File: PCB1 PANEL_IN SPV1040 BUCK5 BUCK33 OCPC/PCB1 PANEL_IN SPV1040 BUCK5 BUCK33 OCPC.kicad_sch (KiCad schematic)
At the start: 0 parts

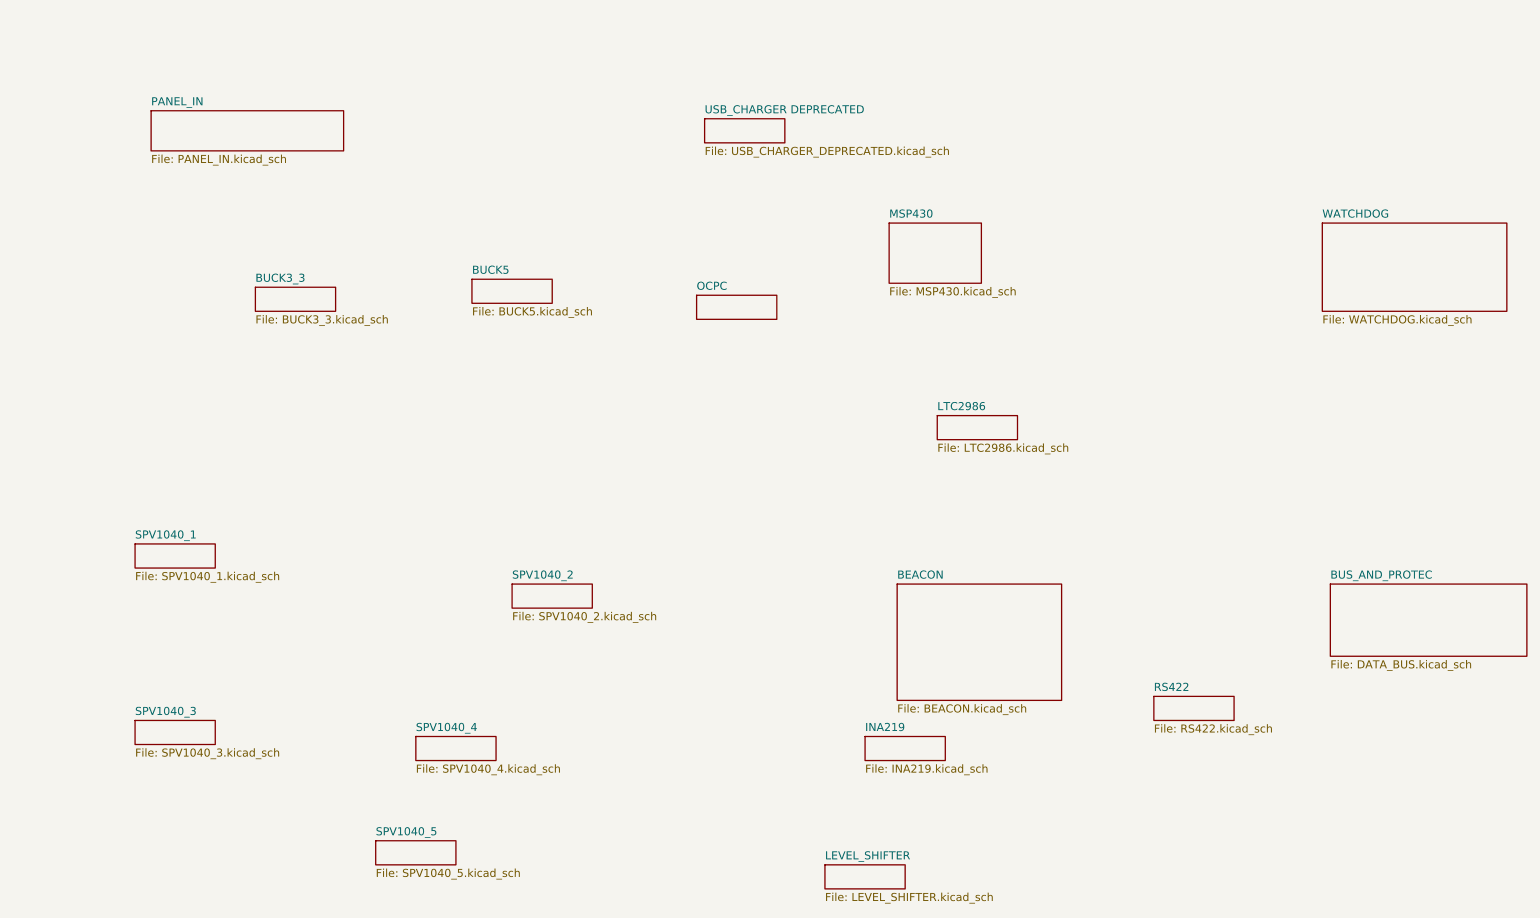
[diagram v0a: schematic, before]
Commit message: Relabeling according to standards
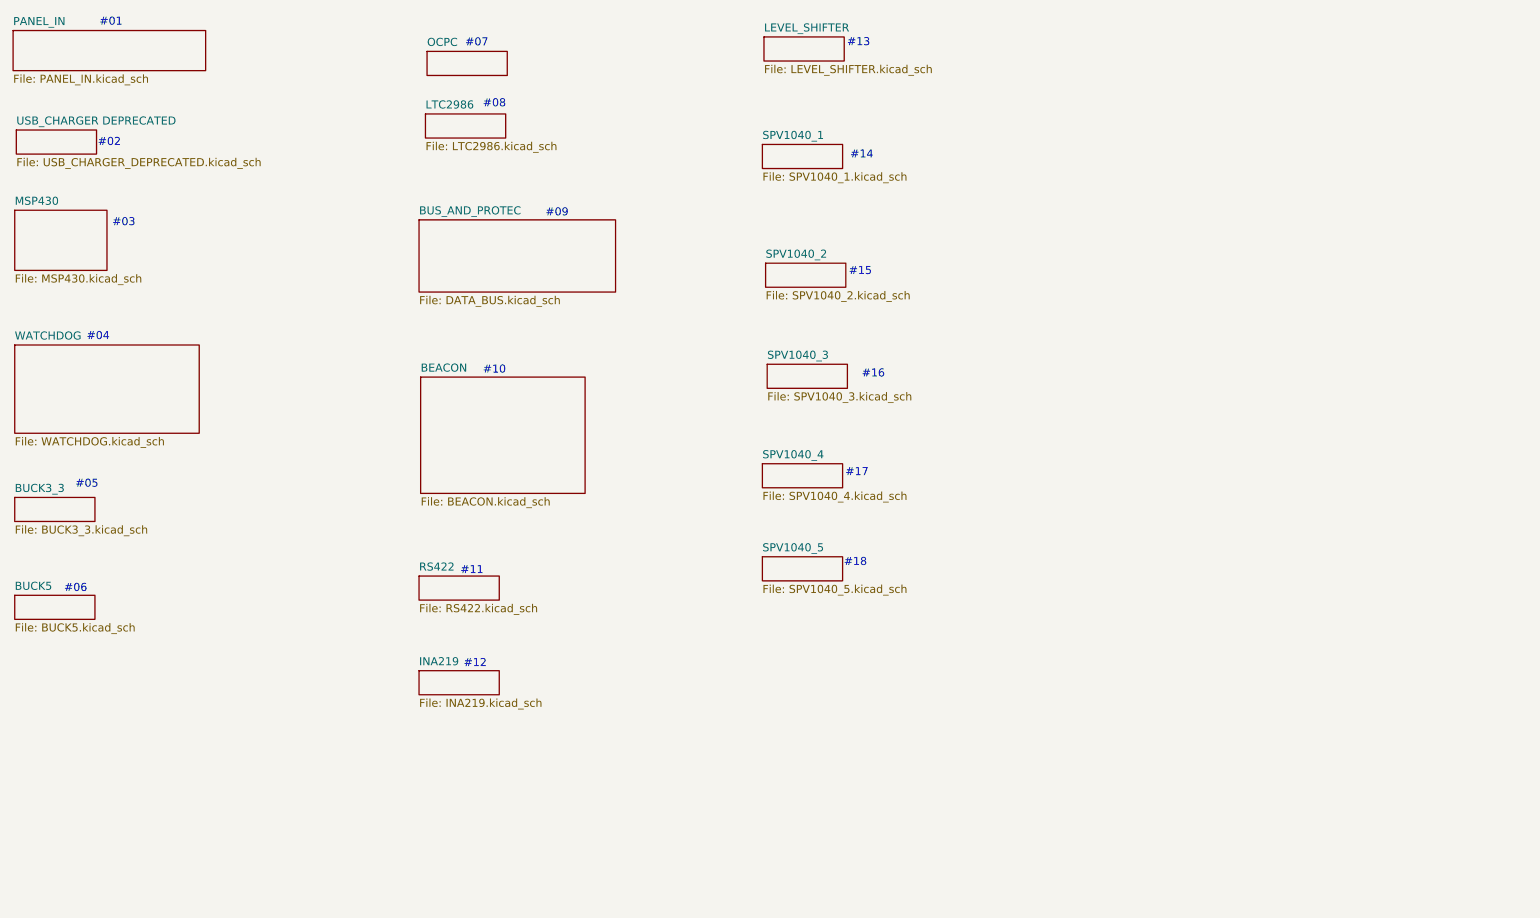
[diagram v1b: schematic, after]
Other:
- note added: "#01"
- note added: "#02"
- note added: "#03"
- note added: "#04"
- note added: "#05"
- note added: "#06"
- note added: "#07"
- note added: "#08"
- note added: "#09"
- note added: "#10"
- note added: "#11"
- note added: "#12"
- note added: "#13"
- note added: "#14"
- note added: "#15"
- note added: "#16"
- note added: "#17"
- note added: "#18"
